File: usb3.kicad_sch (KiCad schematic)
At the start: 46 parts, among them J5 WE_632723300011_alt_symbol, Q4 PJE138K, U17 HD3SS3220, U18 AP22615, U19 TPD4E05U06QDQARQ1, U20 TPD4E05U06QDQARQ1, U21 TPD4E05U06QDQARQ1

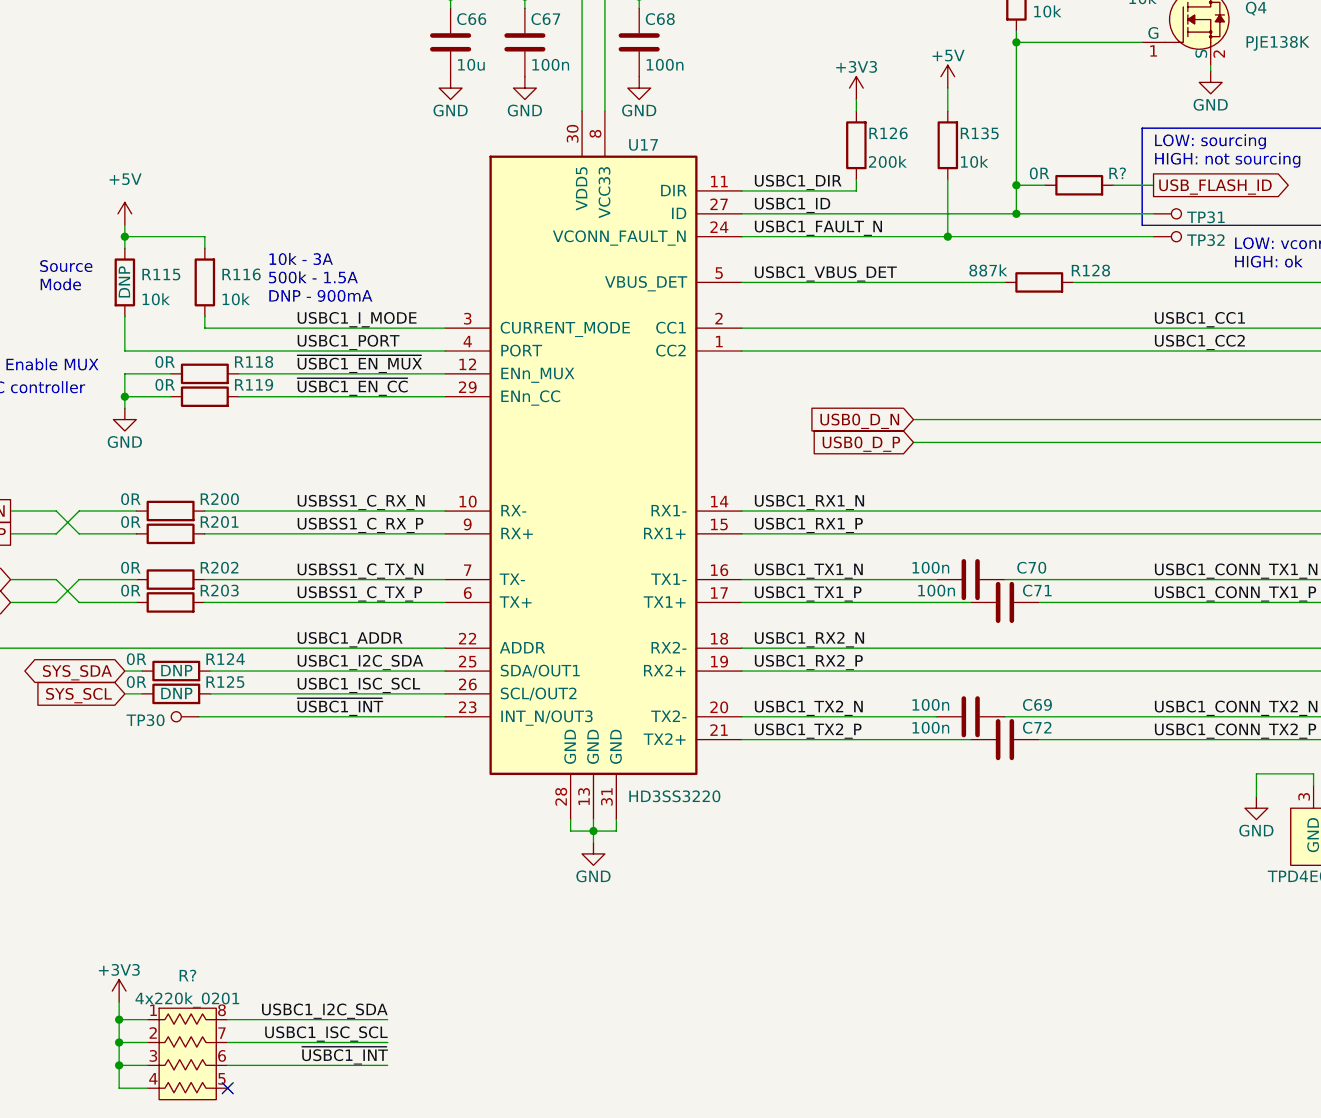
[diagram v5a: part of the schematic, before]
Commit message: Annotate parts, import them on PCB
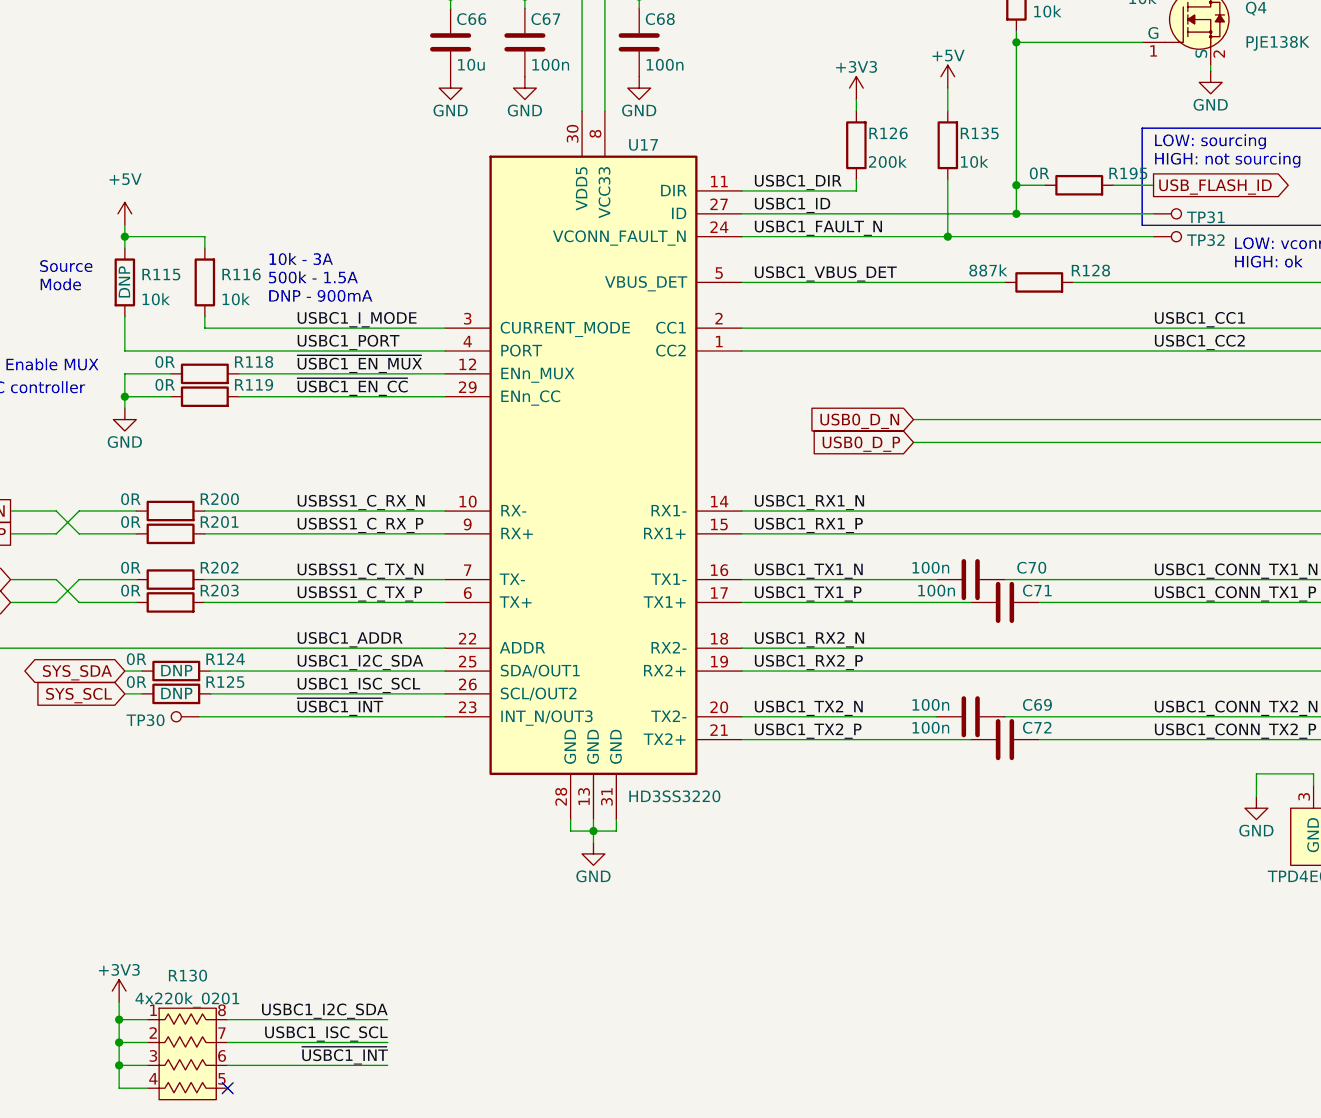
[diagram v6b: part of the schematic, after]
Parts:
- gave numbers to parts that had none: 2
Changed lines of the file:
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@@
   (symbol (lib_id "jetson-orin-baseboard:+3V3") (at 107.315 209.55 0) (unit 1)
     (in_bom yes) (on_board yes) (fields_autoplaced)
-    (property "Reference" "#PWR?" (id 0) (at 107.315 213.36 0)
+    (property "Reference" "#PWR0331" (id 0) (at 107.315 213.36 0)
       (effects (font (size 1.27 1.27)) hide)
     )
@@
   (symbol (lib_id "antmicroResistorNetworksArrays:4x220k_0201_array_1") (at 115.57 221.615 0) (unit 1)
     (in_bom yes) (on_board yes) (fields_autoplaced)
-    (property "Reference" "R?" (id 0) (at 114.935 206.6122 0))
+    (property "Reference" "R130" (id 0) (at 114.935 206.6122 0))
     (property "Value" "4x220k_0201_array_1" (id 1) (at 115.57 224.155 0)
       (effects (font (size 1.524 1.524)) hide)
@@
   (symbol (lib_id "jetson-orin-baseboard:R_0R_0402") (at 213.995 118.745 0) (unit 1)
     (in_bom yes) (on_board yes)
-    (property "Reference" "R?" (id 0) (at 217.17 117.475 0)
-      (effects (font (size 1.27 1.27)) (justify left))
-    )
+    (property "Reference" "R195" (id 0) (at 217.17 117.475 0)
+      (effects (font (size 1.27 1.27)) (justify left))
+    )

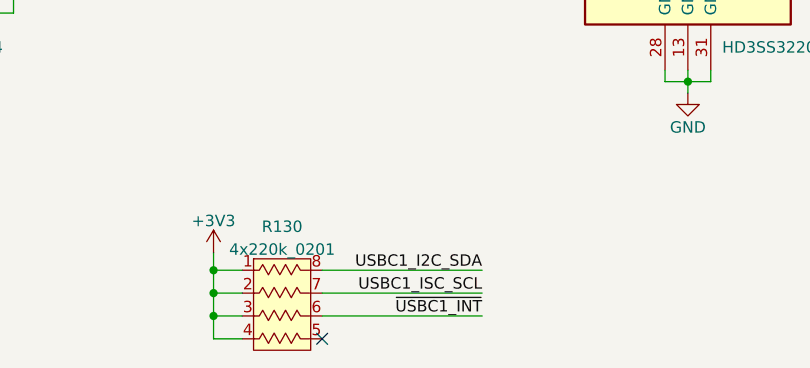
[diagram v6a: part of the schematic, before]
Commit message: Adjust connections on R130 for easier routing
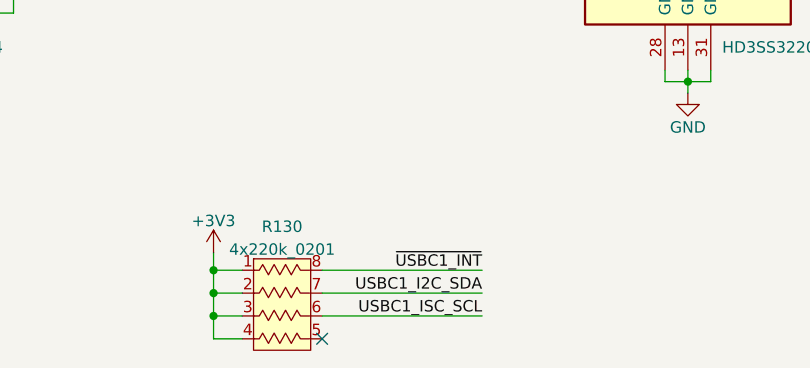
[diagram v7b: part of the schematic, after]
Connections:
- net USBC1_I2C_SDA: now also R130.7; no longer R130.8
- net USBC1_ISC_SCL: now also R130.6; no longer R130.7
- net ~{USBC1_INT}: now also R130.8; no longer R130.6

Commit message: Loclib
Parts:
- Q4: footprint antmicro-footprints:SOT-523 -> jetson-orin-baseboard-footprints:SOT-523; symbol antmicroTransistorsFETsMOSFETsSingle:PJE138K -> jetson-orin-baseboard:PJE138K
- R130: footprint antmicro-footprints:EXB18V -> jetson-orin-baseboard-footprints:EXB18V; symbol antmicroResistorNetworksArrays:4x220k_0201_array_1 -> jetson-orin-baseboard:4x220k_0201_array_1
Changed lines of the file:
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@@
     (pin "1")
   )
-  (symbol (lib_id "antmicroTransistorsFETsMOSFETsSingle:PJE138K") (at 228.6 100.33 0) (unit 1)
+  (symbol (lib_id "jetson-orin-baseboard:PJE138K") (at 228.6 100.33 0) (unit 1)
     (in_bom yes) (on_board yes) (fields_autoplaced)
     (property "Reference" "Q4" (id 0) (at 232.41 99.06 0)
@@
       (effects (font (size 1.27 1.27)) (justify left))
     )
-    (property "Footprint" "antmicro-footprints:SOT-523" (id 2) (at 233.68 95.25 0)
+    (property "Footprint" "jetson-orin-baseboard-footprints:SOT-523" (id 2) (at 233.68 95.25 0)
       (effects (font (size 1.524 1.524)) (justify left) hide)
     )
@@
     (pin "1")
   )
-  (symbol (lib_id "antmicroResistorNetworksArrays:4x220k_0201_array_1") (at 115.57 221.615 0) (unit 1)
+  (symbol (lib_id "jetson-orin-baseboard:4x220k_0201_array_1") (at 115.57 221.615 0) (unit 1)
     (in_bom yes) (on_board yes) (fields_autoplaced)
     (property "Reference" "R130" (id 0) (at 114.935 206.6122 0))
@@
       (effects (font (size 1.524 1.524)) hide)
     )
-    (property "Footprint" "antmicro-footprints:EXB18V" (id 2) (at 110.49 202.565 0)
-      (effects (font (size 1.524 1.524)) (justify left) hide)
-    )
+    (property "Footprint" "jetson-orin-baseboard-footprints:EXB18V" (id 2) (at 110.49 202.565 0)
+      (effects (font (size 1.524 1.524)) (justify left) hide)
+    )
